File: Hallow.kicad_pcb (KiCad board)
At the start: 2 copper layers, 96.6 x 56 mm, 12 parts, among them J1 Screw_Terminal_01x03, J2 Conn_01x06, K1 G5Q-1, P1 Conn_02x20_Odd_Even, Q1 2N3904, U1 WeMos_mini

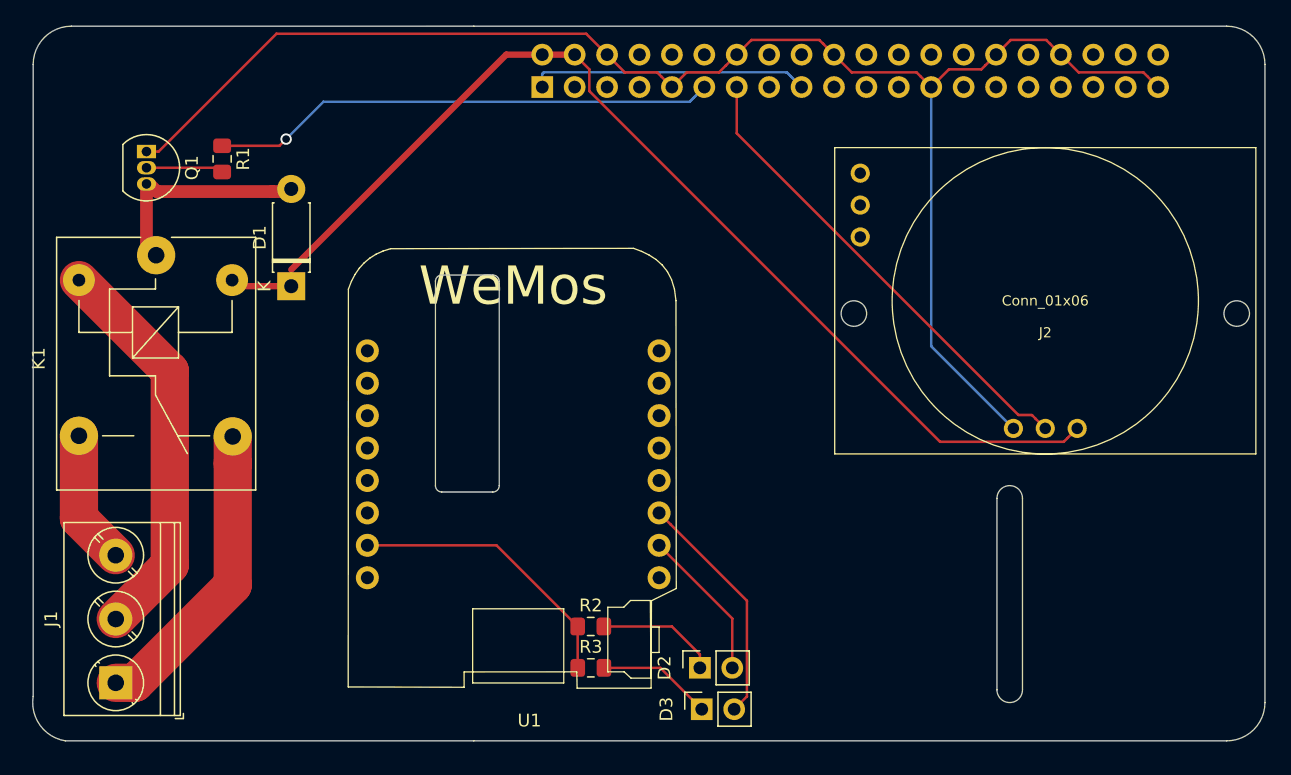
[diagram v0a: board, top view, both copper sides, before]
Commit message: Added Gerbers and added L293D
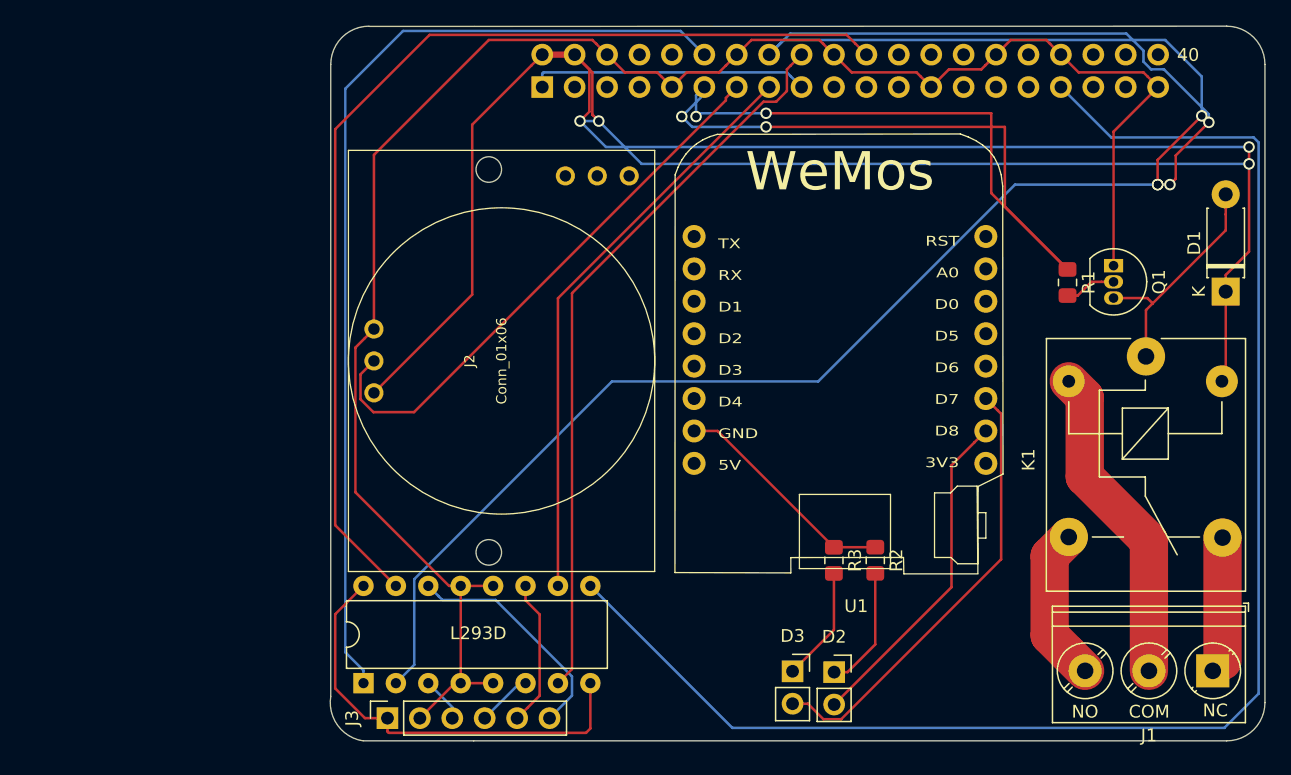
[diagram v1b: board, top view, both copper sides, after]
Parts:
- added G***: LOGO, graphics:goat, B.Cu at (230.4, 122.5)
- added J3: Conn_01x06, Connector_PinSocket_2.54mm:PinSocket_1x06_P2.54mm_Vertical, F.Cu at (196.2, 148.2)
- added L293D: L293D, Package_DIP:DIP-16_W7.62mm, F.Cu at (194.4, 145.5)
- moved J1 86.0 mm to (260.9, 144.5), turned to 180 degrees
- moved K1 78.0 mm to (255.7, 119.9)
- moved Q1 76.3 mm to (253.1, 112.8)
- moved D1 73.2 mm to (261.9, 114.8)
- moved R1 66.9 mm to (249.5, 114.1)
- moved J2 42.9 mm to (205.2, 120.2), turned to 270 degrees
- moved U1 27.1 mm to (231.7, 120.6)
- moved R2 22.9 mm to (234.5, 135.9), turned to 270 degrees
- moved R3 20.8 mm to (231.2, 135.9), turned to 270 degrees
- moved D2 10.5 mm to (231.2, 144.6), turned to 0 degrees
- moved D3 7.71 mm to (228.0, 144.5), turned to 0 degrees
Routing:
- net /GPIO23(GEN4): track 0.00 -> 171.8 mm, vias 0 -> 5
- net /GPIO13(PWM1): track 0.00 -> 118.6 mm
- net +5V: track 88.7 -> 172.9 mm, vias 0 -> 4
- net /GPIO25(GEN6): track 0.00 -> 83.1 mm
- net /GPIO18(GEN1)(PWM0): track 0.00 -> 77.9 mm
- net /GPIO24(GEN5): track 0.00 -> 57.7 mm
- net /GPIO22(GEN3): track 0.00 -> 45.9 mm
- net /GPIO17(GEN0): track 39.7 -> 82.4 mm, vias 1 -> 4
- net /Vcc2: track 0.00 -> 34.7 mm
- net GND: track 120.4 -> 143.6 mm
- net /Out4: track 0.00 -> 18.2 mm
- net /WM_D7: track 18.6 -> 35.1 mm
- net /WM_D8: track 12.0 -> 26.4 mm
- net /RLY(NC): track 24.0 -> 10.8 mm
- net /Out3: track 0.00 -> 11.5 mm
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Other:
- board size 96.6 x 56 mm -> 73.2 x 56 mm
- board text added: "40"
- board text added: "COM"
- board text added: "NC"
- board text added: "NO"
- board text added: "RST A0 D0 D5 D6 D7 D8 3V3"
- board text added: "TX RX D1 D2 D3 D4 GND 5V"
- board text removed: "CAMERA"
- board text removed: "DISPLAY"
